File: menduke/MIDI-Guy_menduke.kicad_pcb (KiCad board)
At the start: 2 copper layers, 88 x 70 mm, 148 parts, among them J1 Jack-DC, J2 SJ-3523-SMT-TR, J3 SJ-3523-SMT-TR, P1 TLP291, U1 TAR5S33, U2 SAM2695, Y1 ABM8G-12.000MHZ-4Y-T3

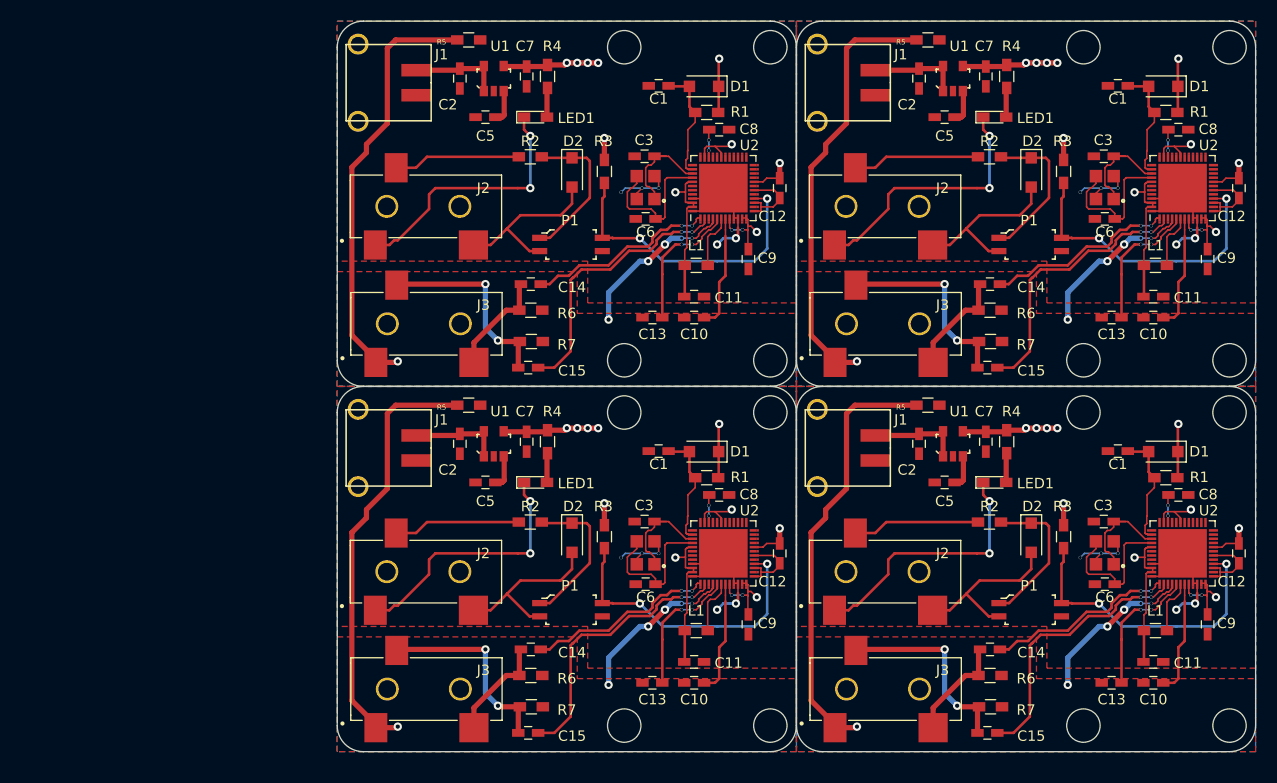
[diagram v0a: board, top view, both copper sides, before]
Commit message: move cap to avoid conflict on panellizing
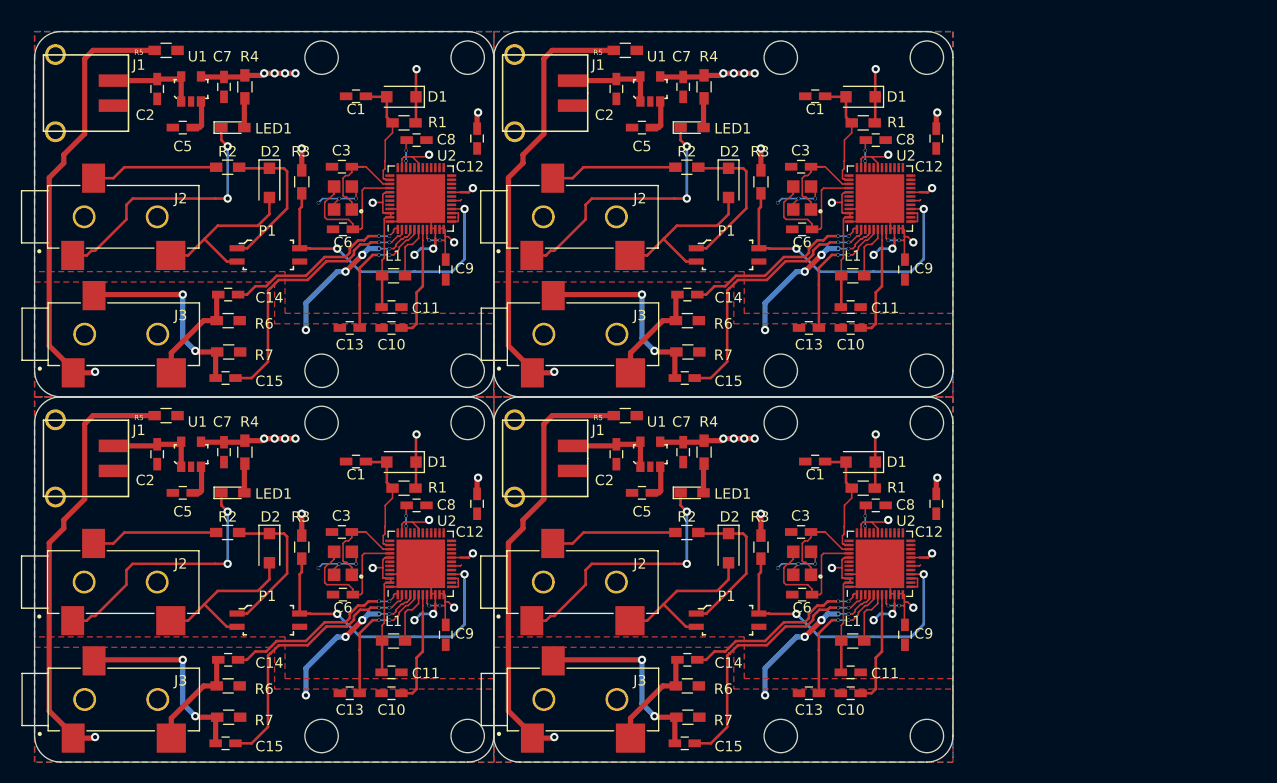
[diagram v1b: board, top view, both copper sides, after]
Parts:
- removed the C1 at (172.8, 92.2)
- removed the C1 at (172.8, 57.2)
- removed the C1 at (128.8, 92.2)
- removed the C10 at (176.2, 114.4)
- removed the C10 at (176.2, 79.4)
- removed the C10 at (132.2, 114.4)
- removed the C11 at (176.2, 112.4)
- removed the C11 at (176.2, 77.4)
- removed the C11 at (132.2, 112.4)
- removed the C12 at (184.4, 102.0)
- removed the C12 at (184.4, 67.0)
- removed the C12 at (140.4, 102.0)
- removed the C13 at (172.2, 114.4)
- removed the C13 at (172.2, 79.4)
- removed the C13 at (128.2, 114.4)
- removed the C14 at (160.6, 111.2)
- removed the C14 at (160.6, 76.2)
- removed the C14 at (116.5, 111.2)
- removed the C15 at (160.3, 119.2)
- removed the C15 at (160.3, 84.2)
- removed the C15 at (116.3, 119.2)
- removed the C2 at (153.8, 91.5)
- removed the C2 at (153.8, 56.5)
- removed the C2 at (109.8, 91.5)
- removed the C3 at (171.4, 99.0)
- removed the C3 at (171.4, 64.0)
- removed the C3 at (127.5, 99.0)
- removed the C5 at (156.2, 95.2)
- removed the C5 at (156.2, 60.2)
- removed the C5 at (112.2, 95.2)
- removed the C6 at (171.6, 105.0)
- removed the C6 at (171.6, 70.0)
- removed the C6 at (127.5, 105.0)
- removed the C7 at (160.2, 91.3)
- removed the C7 at (160.2, 56.3)
- removed the C7 at (116.2, 91.3)
- removed the C8 at (178.6, 96.4)
- removed the C8 at (178.6, 61.4)
- removed the C8 at (134.6, 96.4)
- removed the C9 at (181.4, 108.8)
- removed the C9 at (181.4, 73.8)
- removed the C9 at (137.4, 108.8)
- removed the D1 at (177.2, 92.2)
- removed the D1 at (177.2, 57.2)
- removed the D1 at (133.2, 92.2)
- removed the D2 at (164.5, 100.5)
- removed the D2 at (164.5, 65.5)
- removed the D2 at (120.5, 100.5)
- removed the G*** at (181.0, 107.0)
- removed the G*** at (181.0, 72.0)
- removed the G*** at (137.0, 107.0)
- removed the J1 at (151.0, 91.9)
- removed the J1 at (151.0, 56.9)
- removed the J1 at (107.0, 91.9)
- removed the J2 at (146.8, 103.8)
- removed the J2 at (146.8, 68.8)
- removed the J2 at (102.8, 103.8)
- removed the J3 at (146.8, 115.0)
- removed the J3 at (146.8, 80.0)
- removed the J3 at (102.8, 115.0)
- removed the L1 at (176.4, 109.4)
- removed the L1 at (176.4, 74.4)
- removed the L1 at (132.4, 109.4)
- removed the LED1 at (161.0, 95.2)
- removed the LED1 at (161.0, 60.2)
- removed the LED1 at (117.0, 95.2)
- removed the P1 at (164.4, 107.4)
- removed the P1 at (164.4, 72.4)
- removed the P1 at (120.4, 107.4)
- removed the R1 at (177.4, 94.8)
- removed the R1 at (177.4, 59.8)
- removed the R1 at (133.4, 94.8)
- removed the R2 at (160.5, 99.0)
- removed the R2 at (160.5, 64.0)
- removed the R2 at (116.5, 99.0)
- removed the R3 at (167.6, 100.4)
- removed the R3 at (167.6, 65.4)
- removed the R3 at (123.6, 100.4)
- removed the R4 at (162.2, 91.3)
- removed the R4 at (162.2, 56.3)
- removed the R4 at (118.2, 91.3)
- removed the R5 at (154.6, 87.8)
- removed the R5 at (154.6, 52.8)
- removed the R5 at (110.6, 87.8)
- removed the R6 at (160.6, 113.7)
- removed the R6 at (160.6, 78.7)
- removed the R6 at (116.5, 113.7)
- removed the R7 at (160.6, 116.7)
- removed the R7 at (160.6, 81.7)
- removed the R7 at (116.6, 116.7)
- removed the REF** at (169.5, 88.5)
- removed the REF** at (183.5, 88.5)
- removed the REF** at (183.5, 53.5)
- removed the REF** at (139.5, 88.5)
- removed the REF** at (125.5, 53.5)
- removed the REF** at (125.5, 83.5)
- removed the REF** at (139.5, 83.5)
- removed the REF** at (169.5, 53.5)
- removed the REF** at (125.5, 88.5)
- removed the REF** at (183.5, 118.5)
- removed the REF** at (183.5, 83.5)
- removed the REF** at (139.5, 118.5)
- removed the REF** at (169.5, 118.5)
- removed the REF** at (169.5, 83.5)
- removed the REF** at (125.5, 118.5)
- removed the U1 at (157.0, 91.5)
- removed the U1 at (157.0, 56.5)
- removed the U1 at (113.0, 91.5)
- removed the U2 at (179.0, 102.0)
- removed the U2 at (179.0, 67.0)
- removed the U2 at (135.0, 102.0)
- removed the Y1 at (171.6, 102.0)
- removed the Y1 at (171.6, 67.0)
- removed the Y1 at (127.5, 102.0)
- added C1: 1u, Capacitors_SMD:C_0603_HandSoldering, F.Cu at (143.8, 93.2)
- added C1: 1u, Capacitors_SMD:C_0603_HandSoldering, F.Cu at (99.8, 93.2)
- added C1: 1u, Capacitors_SMD:C_0603_HandSoldering, F.Cu at (143.8, 58.2)
- added C10: 1u, Capacitors_SMD:C_0603_HandSoldering, F.Cu at (147.2, 115.4)
- added C10: 1u, Capacitors_SMD:C_0603_HandSoldering, F.Cu at (103.2, 115.4)
- added C10: 1u, Capacitors_SMD:C_0603_HandSoldering, F.Cu at (147.2, 80.4)
- added C11: 0.1u, Capacitors_SMD:C_0603_HandSoldering, F.Cu at (147.2, 113.4)
- added C11: 0.1u, Capacitors_SMD:C_0603_HandSoldering, F.Cu at (103.2, 113.4)
- added C11: 0.1u, Capacitors_SMD:C_0603_HandSoldering, F.Cu at (147.2, 78.4)
- added C12: 0.1u, Capacitors_SMD:C_0603_HandSoldering, F.Cu at (155.4, 97.2)
- added C12: 0.1u, Capacitors_SMD:C_0603_HandSoldering, F.Cu at (111.4, 97.2)
- added C12: 0.1u, Capacitors_SMD:C_0603_HandSoldering, F.Cu at (155.4, 62.2)
- added C13: 0.1u, Capacitors_SMD:C_0603_HandSoldering, F.Cu at (143.2, 115.4)
- added C13: 0.1u, Capacitors_SMD:C_0603_HandSoldering, F.Cu at (99.2, 115.4)
- added C13: 0.1u, Capacitors_SMD:C_0603_HandSoldering, F.Cu at (143.2, 80.4)
- added C14: 10u, Capacitors_SMD:C_0603_HandSoldering, F.Cu at (131.6, 112.2)
- added C14: 10u, Capacitors_SMD:C_0603_HandSoldering, F.Cu at (87.5, 112.2)
- added C14: 10u, Capacitors_SMD:C_0603_HandSoldering, F.Cu at (131.6, 77.2)
- added C15: 10u, Capacitors_SMD:C_0603_HandSoldering, F.Cu at (131.3, 120.2)
- added C15: 10u, Capacitors_SMD:C_0603_HandSoldering, F.Cu at (87.3, 120.2)
- added C15: 10u, Capacitors_SMD:C_0603_HandSoldering, F.Cu at (131.3, 85.2)
- added C2: 10u, Capacitors_SMD:C_0603_HandSoldering, F.Cu at (124.8, 92.5)
- added C2: 10u, Capacitors_SMD:C_0603_HandSoldering, F.Cu at (80.8, 92.5)
- added C2: 10u, Capacitors_SMD:C_0603_HandSoldering, F.Cu at (124.8, 57.5)
- added C3: 10p, Capacitors_SMD:C_0603_HandSoldering, F.Cu at (142.4, 100.0)
- added C3: 10p, Capacitors_SMD:C_0603_HandSoldering, F.Cu at (98.5, 100.0)
- added C3: 10p, Capacitors_SMD:C_0603_HandSoldering, F.Cu at (142.4, 65.0)
- added C5: 0.01u, Capacitors_SMD:C_0603_HandSoldering, F.Cu at (127.2, 96.2)
- added C5: 0.01u, Capacitors_SMD:C_0603_HandSoldering, F.Cu at (83.2, 96.2)
- added C5: 0.01u, Capacitors_SMD:C_0603_HandSoldering, F.Cu at (127.2, 61.2)
- added C6: 10p, Capacitors_SMD:C_0603_HandSoldering, F.Cu at (142.6, 106.0)
- added C6: 10p, Capacitors_SMD:C_0603_HandSoldering, F.Cu at (98.5, 106.0)
- added C6: 10p, Capacitors_SMD:C_0603_HandSoldering, F.Cu at (142.6, 71.0)
- added C7: 10u, Capacitors_SMD:C_0603_HandSoldering, F.Cu at (131.2, 92.3)
- added C7: 10u, Capacitors_SMD:C_0603_HandSoldering, F.Cu at (87.2, 92.3)
- added C7: 10u, Capacitors_SMD:C_0603_HandSoldering, F.Cu at (131.2, 57.3)
- added C8: 4.7u, Capacitors_SMD:C_0603_HandSoldering, F.Cu at (149.6, 97.4)
- added C8: 4.7u, Capacitors_SMD:C_0603_HandSoldering, F.Cu at (105.6, 97.4)
- added C8: 4.7u, Capacitors_SMD:C_0603_HandSoldering, F.Cu at (149.6, 62.4)
- added C9: 0.1u, Capacitors_SMD:C_0603_HandSoldering, F.Cu at (152.4, 109.8)
- added C9: 0.1u, Capacitors_SMD:C_0603_HandSoldering, F.Cu at (108.4, 109.8)
- added C9: 0.1u, Capacitors_SMD:C_0603_HandSoldering, F.Cu at (152.4, 74.8)
- added D1: GS1010FL, Diodes_SMD:D_SOD-123F, F.Cu at (148.2, 93.2)
- added D1: GS1010FL, Diodes_SMD:D_SOD-123F, F.Cu at (104.2, 93.2)
- added D1: GS1010FL, Diodes_SMD:D_SOD-123F, F.Cu at (148.2, 58.2)
- added D2: GS1010FL, Diodes_SMD:D_SOD-123F, F.Cu at (135.5, 101.5)
- added D2: GS1010FL, Diodes_SMD:D_SOD-123F, F.Cu at (91.5, 101.5)
- added D2: GS1010FL, Diodes_SMD:D_SOD-123F, F.Cu at (135.5, 66.5)
- added G***: LOGO, mylib:kinoshita-logo, B.Cu at (152.0, 108.0)
- added G***: LOGO, mylib:kinoshita-logo, B.Cu at (108.0, 108.0)
- added G***: LOGO, mylib:kinoshita-logo, B.Cu at (152.0, 73.0)
- added J1: Jack-DC, mylib:MRUSB-2B-D14NI-S306, F.Cu at (122.0, 92.9)
- added J1: Jack-DC, mylib:MRUSB-2B-D14NI-S306, F.Cu at (78.0, 92.9)
- added J1: Jack-DC, mylib:MRUSB-2B-D14NI-S306, F.Cu at (122.0, 57.9)
- added J2: SJ-3523-SMT-TR, snapeda:CUI_SJ-3523-SMT-TR, F.Cu at (117.8, 104.8)
- added J2: SJ-3523-SMT-TR, snapeda:CUI_SJ-3523-SMT-TR, F.Cu at (73.8, 104.8)
- added J2: SJ-3523-SMT-TR, snapeda:CUI_SJ-3523-SMT-TR, F.Cu at (117.8, 69.8)
- added J3: SJ-3523-SMT-TR, snapeda:CUI_SJ-3523-SMT-TR, F.Cu at (117.8, 116.0)
- added J3: SJ-3523-SMT-TR, snapeda:CUI_SJ-3523-SMT-TR, F.Cu at (73.8, 116.0)
- added J3: SJ-3523-SMT-TR, snapeda:CUI_SJ-3523-SMT-TR, F.Cu at (117.8, 81.0)
- added L1: BLM18P, Inductors_SMD:L_0603_HandSoldering, F.Cu at (147.4, 110.4)
- added L1: BLM18P, Inductors_SMD:L_0603_HandSoldering, F.Cu at (103.4, 110.4)
- added L1: BLM18P, Inductors_SMD:L_0603_HandSoldering, F.Cu at (147.4, 75.4)
- added LED1: LED, LEDs:LED_0603_HandSoldering, F.Cu at (132.0, 96.2)
- added LED1: LED, LEDs:LED_0603_HandSoldering, F.Cu at (88.0, 96.2)
- added LED1: LED, LEDs:LED_0603_HandSoldering, F.Cu at (132.0, 61.2)
- added P1: TLP291, mylib:TLP291, F.Cu at (135.4, 108.4)
- added P1: TLP291, mylib:TLP291, F.Cu at (91.4, 108.4)
- added P1: TLP291, mylib:TLP291, F.Cu at (135.4, 73.4)
- added R1: 10k, Resistors_SMD:R_0603_HandSoldering, F.Cu at (148.4, 95.8)
- added R1: 10k, Resistors_SMD:R_0603_HandSoldering, F.Cu at (104.4, 95.8)
- added R1: 10k, Resistors_SMD:R_0603_HandSoldering, F.Cu at (148.4, 60.8)
- added R2: 220, Resistors_SMD:R_0603_HandSoldering, F.Cu at (131.5, 100.0)
- added R2: 220, Resistors_SMD:R_0603_HandSoldering, F.Cu at (87.5, 100.0)
- added R2: 220, Resistors_SMD:R_0603_HandSoldering, F.Cu at (131.5, 65.0)
- added R3: 470?, Resistors_SMD:R_0603_HandSoldering, F.Cu at (138.6, 101.4)
- added R3: 470?, Resistors_SMD:R_0603_HandSoldering, F.Cu at (94.6, 101.4)
- added R3: 470?, Resistors_SMD:R_0603_HandSoldering, F.Cu at (138.6, 66.4)
- added R4: 1k, Resistors_SMD:R_0603_HandSoldering, F.Cu at (133.2, 92.3)
- added R4: 1k, Resistors_SMD:R_0603_HandSoldering, F.Cu at (89.2, 92.3)
- added R4: 1k, Resistors_SMD:R_0603_HandSoldering, F.Cu at (133.2, 57.3)
- added R5: 0, Resistors_SMD:R_0603_HandSoldering, F.Cu at (125.6, 88.8)
- added R5: 0, Resistors_SMD:R_0603_HandSoldering, F.Cu at (81.6, 88.8)
- added R5: 0, Resistors_SMD:R_0603_HandSoldering, F.Cu at (125.6, 53.8)
- added R6: 47k, Resistors_SMD:R_0603_HandSoldering, F.Cu at (131.6, 114.7)
- added R6: 47k, Resistors_SMD:R_0603_HandSoldering, F.Cu at (87.5, 114.7)
- added R6: 47k, Resistors_SMD:R_0603_HandSoldering, F.Cu at (131.6, 79.7)
- added R7: 47k, Resistors_SMD:R_0603_HandSoldering, F.Cu at (131.6, 117.7)
- added R7: 47k, Resistors_SMD:R_0603_HandSoldering, F.Cu at (87.6, 117.7)
- added R7: 47k, Resistors_SMD:R_0603_HandSoldering, F.Cu at (131.6, 82.7)
- added REF**: MountingHole_3.2mm_M3_DIN965, Mounting_Holes:MountingHole_3.2mm_M3_DIN965, F.Cu at (154.5, 89.5)
- added REF**: MountingHole_3.2mm_M3_DIN965, Mounting_Holes:MountingHole_3.2mm_M3_DIN965, F.Cu at (154.5, 119.5)
- added REF**: MountingHole_3.2mm_M3_DIN965, Mounting_Holes:MountingHole_3.2mm_M3_DIN965, F.Cu at (110.5, 119.5)
- added REF**: MountingHole_3.2mm_M3_DIN965, Mounting_Holes:MountingHole_3.2mm_M3_DIN965, F.Cu at (154.5, 84.5)
- added REF**: MountingHole_3.2mm_M3_DIN965, Mounting_Holes:MountingHole_3.2mm_M3_DIN965, F.Cu at (96.5, 54.5)
- added REF**: MountingHole_3.2mm_M3_DIN965, Mounting_Holes:MountingHole_3.2mm_M3_DIN965, F.Cu at (96.5, 84.5)
- added REF**: MountingHole_3.2mm_M3_DIN965, Mounting_Holes:MountingHole_3.2mm_M3_DIN965, F.Cu at (110.5, 84.5)
- added REF**: MountingHole_3.2mm_M3_DIN965, Mounting_Holes:MountingHole_3.2mm_M3_DIN965, F.Cu at (110.5, 89.5)
- added REF**: MountingHole_3.2mm_M3_DIN965, Mounting_Holes:MountingHole_3.2mm_M3_DIN965, F.Cu at (154.5, 54.5)
- added REF**: MountingHole_3.2mm_M3_DIN965, Mounting_Holes:MountingHole_3.2mm_M3_DIN965, F.Cu at (140.5, 89.5)
- added REF**: MountingHole_3.2mm_M3_DIN965, Mounting_Holes:MountingHole_3.2mm_M3_DIN965, F.Cu at (96.5, 89.5)
- added REF**: MountingHole_3.2mm_M3_DIN965, Mounting_Holes:MountingHole_3.2mm_M3_DIN965, F.Cu at (140.5, 54.5)
- added REF**: MountingHole_3.2mm_M3_DIN965, Mounting_Holes:MountingHole_3.2mm_M3_DIN965, F.Cu at (140.5, 119.5)
- added REF**: MountingHole_3.2mm_M3_DIN965, Mounting_Holes:MountingHole_3.2mm_M3_DIN965, F.Cu at (96.5, 119.5)
- added REF**: MountingHole_3.2mm_M3_DIN965, Mounting_Holes:MountingHole_3.2mm_M3_DIN965, F.Cu at (140.5, 84.5)
- added U1: TAR5S33, mylib:TAR5S33_Akizuki_Toshiba_SSOP5, F.Cu at (128.0, 92.5)
- added U1: TAR5S33, mylib:TAR5S33_Akizuki_Toshiba_SSOP5, F.Cu at (84.0, 92.5)
- added U1: TAR5S33, mylib:TAR5S33_Akizuki_Toshiba_SSOP5, F.Cu at (128.0, 57.5)
- added U2: SAM2695, mylib:SAM2695_QFN-48-6x6mm_Pitch0.4mm, F.Cu at (150.0, 103.0)
- added U2: SAM2695, mylib:SAM2695_QFN-48-6x6mm_Pitch0.4mm, F.Cu at (106.0, 103.0)
- added U2: SAM2695, mylib:SAM2695_QFN-48-6x6mm_Pitch0.4mm, F.Cu at (150.0, 68.0)
- added Y1: ABM8G-12.000MHZ-4Y-T3, snapeda:OSCSC320X250X100N, F.Cu at (142.6, 103.0)
- added Y1: ABM8G-12.000MHZ-4Y-T3, snapeda:OSCSC320X250X100N, F.Cu at (98.5, 103.0)
- added Y1: ABM8G-12.000MHZ-4Y-T3, snapeda:OSCSC320X250X100N, F.Cu at (142.6, 68.0)
- moved C12 29.4 mm to (111.4, 62.2)
- moved C1 29.0 mm to (99.8, 58.2)
- moved C14 29.0 mm to (87.5, 77.2)
- moved C15 29.0 mm to (87.3, 85.2)
- moved C2 29.0 mm to (80.8, 57.5)
- moved C3 29.0 mm to (98.5, 65.0)
- moved C5 29.0 mm to (83.2, 61.2)
- moved C6 29.0 mm to (98.5, 71.0)
- moved C7 29.0 mm to (87.2, 57.3)
- moved C8 29.0 mm to (105.6, 62.4)
- moved C9 29.0 mm to (108.4, 74.8)
- moved D1 29.0 mm to (104.2, 58.2)
- moved D2 29.0 mm to (91.5, 66.5)
- moved G*** 29.0 mm to (108.0, 73.0)
- moved J1 29.0 mm to (78.0, 57.9)
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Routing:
- net GND: track 214.6 -> 197.9 mm
- net +3V3: track 189.3 -> 188.3 mm, vias 48 -> 52
